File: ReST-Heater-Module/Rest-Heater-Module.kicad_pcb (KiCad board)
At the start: 2 copper layers, 17.4 x 34.4 mm, 62 parts, among them P1 CONN_02X02, P2 CONN_02X05, P3 02-SCREW-TERM, P4 01X02-MALE, P5 02-SCREW-TERM, Q1 Q_BSH105, Q2 Q_AOT240L

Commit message: Save of work
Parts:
- added JP***: bb02-hp04, ReST-Library:bb02-hp04, B.Cu at (144.0, 109.6)
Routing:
- net +12V: track 49.9 -> 2.49 mm
- added copper zone on B.Cu, net +12V
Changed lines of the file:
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@@
 (kicad_pcb (version 4) (host pcbnew 4.0.2-stable)
   (general
-    (links 79)
+    (links 83)
     (no_connects 0)
     (area 140.794999 97.794999 158.205001 132.205001)
     (thickness 1.6)
     (drawings 14)
-    (tracks 158)
+    (tracks 140)
     (zones 0)
-    (modules 62)
+    (modules 63)
     (nets 11)
   )
@@
   )
   (setup
-    (last_trace_width 0.3)
+    (last_trace_width 0.25)
     (user_trace_width 0.2)
     (user_trace_width 0.3)
@@
     (mod_text_size 1 1)
     (mod_text_width 0.15)
-    (pad_size 0.5 0.5)
-    (pad_drill 0.4)
+    (pad_size 1.02 3.45)
+    (pad_drill 0)
     (pad_to_mask_clearance 0)
     (aux_axis_origin 0 0)
@@
     )
     (model ../../../../../../Users/Matjas/Documents/Git/RepRapSTM32duinoDriver/3D-Models/conn_mpt/mpt_0,5-2-2,54.wrl
+      (at (xyz 0 0 0))
+      (scale (xyz 1 1 1))
+      (rotate (xyz 0 0 0))
+    )
+  )
+  (module ReST-Library:bb02-hp04 (layer B.Cu)
+    (at 144 109.6)
+    (descr "Smd dual-row strip connector, 2x2 pin, 2.54mm pitch")
+    (fp_text reference JP*** (at 0 5.2) (layer B.SilkS)
+      (effects (font (size 0.99822 0.99822) (thickness 0.19812)) (justify mirror))
+    )
+    (fp_text value bb02-hp04 (at 0 -5.5) (layer B.SilkS)
+      (effects (font (size 0.99568 0.99568) (thickness 0.19558)) (justify mirror))
+    )
+    (fp_text user 1 (at -1.2 -0.4 270) (layer B.SilkS)
+      (effects (font (size 1 1) (thickness 0.15)) (justify mirror))
+    )
+    (fp_line (start -2.6 2.6) (end 2.6 2.6) (layer B.SilkS) (width 0.19812))
+    (fp_line (start 2.6 2.6) (end 2.6 -2.6) (layer B.SilkS) (width 0.19812))
+    (fp_line (start 2.6 -2.6) (end -2.6 -2.6) (layer B.SilkS) (width 0.19812))
+    (fp_line (start -2.6 -2.6) (end -2.6 2.6) (layer B.SilkS) (width 0.19812))
+    (pad 1 smd rect (at -1.27 -2.725) (size 1.02 3.45) (layers B.Cu B.Paste B.Mask)
+      (net 5 +12V))
+    (pad 2 smd rect (at -1.27 2.725) (size 1.02 3.45) (layers B.Cu B.Paste B.Mask)
+      (net 5 +12V))
+    (pad 3 smd rect (at 1.27 -2.725) (size 1.02 3.45) (layers B.Cu B.Paste B.Mask)
+      (net 5 +12V))
+    (pad 4 smd rect (at 1.27 2.725) (size 1.02 3.45) (layers B.Cu B.Paste B.Mask)
+      (net 5 +12V))
+    (model walter/smd_strip/BB02-HP04.wrl
       (at (xyz 0 0 0))
       (scale (xyz 1 1 1))
@@
   (segment (start 147.41986 124.41986) (end 144.10008 121.10008) (width 0.3) (layer F.Cu) (net 4))
   (segment (start 144.10008 121.10008) (end 144 121.10008) (width 0.3) (layer F.Cu) (net 4))
-  (segment (start 149.5095 122.9595) (end 150 122.9595) (width 3) (layer B.Cu) (net 5))
-  (segment (start 150 122.9595) (end 149.5095 122.9595) (width 3) (layer B.Cu) (net 5))
-  (segment (start 149.5095 122.9595) (end 144.92254 118.37254) (width 3) (layer B.Cu) (net 5))
   (via (at 144.45 123.15) (size 0.6) (drill 0.4) (layers F.Cu B.Cu) (net 5))
   (segment (start 144.45 123.15) (end 144.6405 122.9595) (width 1.5) (layer B.Cu) (net 5))
   (segment (start 144.6405 122.9595) (end 144.92254 122.9595) (width 1.5) (layer B.Cu) (net 5))
-  (segment (start 147.46 115.53) (end 147.46 120.91) (width 3) (layer B.Cu) (net 5))
-  (segment (start 147.46 120.91) (end 149.5095 122.9595) (width 3) (layer B.Cu) (net 5))
-  (segment (start 147.46 122.9595) (end 150 122.9595) (width 3) (layer B.Cu) (net 5))
-  (segment (start 144.92254 122.9595) (end 144.92254 118.37254) (width 3) (layer B.Cu) (net 5))
-  (segment (start 144.92254 118.37254) (end 144.92254 116.62254) (width 3) (layer B.Cu) (net 5))
-  (segment (start 144.92254 116.62254) (end 144.9 116.64508) (width 3) (layer B.Cu) (net 5))
-  (segment (start 144.9 116.64508) (end 144.9 118.5) (width 3) (layer B.Cu) (net 5))
-  (segment (start 147.46 122.9595) (end 144.92254 122.9595) (width 3) (layer B.Cu) (net 5))
-  (segment (start 144.92 115.53) (end 144.92 118.5) (width 5) (layer B.Cu) (net 5))
-  (segment (start 144.92 118.5) (end 144.92 116.62) (width 5) (layer B.Cu) (net 5))
-  (segment (start 144.92 115.53) (end 144.92 115.47) (width 5) (layer B.Cu) (net 5))
-  (segment (start 144.92 115.47) (end 144.05 114.6) (width 5) (layer B.Cu) (net 5))
   (segment (start 144 124.89992) (end 144 123.6) (width 1.5) (layer F.Cu) (net 5))
   (segment (start 144 123.6) (end 144.45 123.15) (width 1.5) (layer F.Cu) (net 5))
-  (segment (start 144.9 118.5) (end 144.92 118.5) (width 3) (layer B.Cu) (net 5))
-  (segment (start 144.05 114.6) (end 144.05 102.7) (width 5) (layer B.Cu) (net 5))
-  (segment (start 144.05 102.7) (end 144.25 102.5) (width 5) (layer B.Cu) (net 5))
   (segment (start 145.925 131.35) (end 144.475 131.35) (width 0.3) (layer B.Cu) (net 6))
   (segment (start 144.4 125.8) (end 144.975 125.225) (width 0.3) (layer B.Cu) (net 6))
@@
     (connect_pads (clearance 0.35))
     (min_thickness 0.254)
-    (fill yes (arc_segments 16) (thermal_gap 0.508) (thermal_bridge_width 1))
+    (fill yes (arc_segments 16) (thermal_gap 0.508) (thermal_bridge_width 2))
     (polygon
       (pts
@@
     (connect_pads (clearance 0.35))
     (min_thickness 0.254)
-    (fill yes (arc_segments 16) (thermal_gap 0.508) (thermal_bridge_width 1))
+    (fill yes (arc_segments 16) (thermal_gap 0.508) (thermal_bridge_width 2))
     (polygon
       (pts
@@
       )
     )
+  )
+  (zone (net 5) (net_name +12V) (layer B.Cu) (hatch edge 0.508)
+    (priority 1)
+    (connect_pads yes (clearance 0.35))
+    (min_thickness 0.254)
+    (fill yes (arc_segments 16) (thermal_gap 0.508) (thermal_bridge_width 2))
+    (polygon
+      (pts
+        (xy 151 124.2) (xy 142.2 124.2) (xy 142.2 116.4) (xy 141.6 115.8) (xy 141.6 101.2)
+        (xy 143.2 99.6) (xy 145.6 99.6) (xy 147 101) (xy 147 104.2) (xy 146.6 104.6)
+        (xy 146.6 113) (xy 147.4 113.8) (xy 148.6 113.8) (xy 148.6 119.2) (xy 151 119.2)
+      )
+    )

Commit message: finishing touches on Heater and Stepper Modules
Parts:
- C1: value 10uF -> (none)
- D1: value LED -> (none)
- D2: value D_1N400x-SMD -> (none)
- P1: value CONN_02X02 -> (none)
- P3, P5: value 02-SCREW-TERM -> (none)
- P4: value 01X02-MALE -> (none)
- Q1: value Q_BSH105 -> (none)
- Q2: value Q_AOT240L -> (none)
- R1: value 4.7K -> (none)
- R2, R3: value 100K -> (none)
- R4: value 22R -> (none)
- R5: value 1K -> (none)
- renumbered JP*** to P7

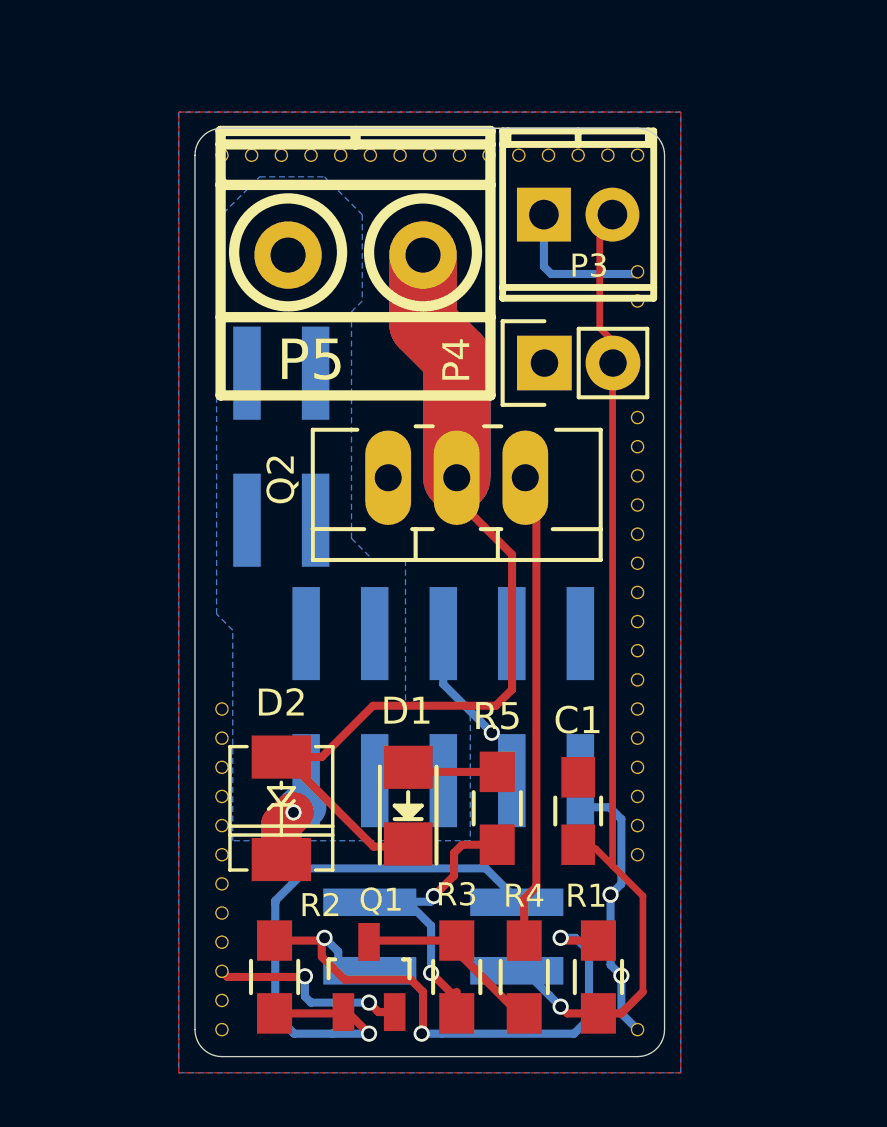
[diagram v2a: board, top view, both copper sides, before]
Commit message: Changes in Heatbed and Heater + F1 and F4 Pinout table with functions
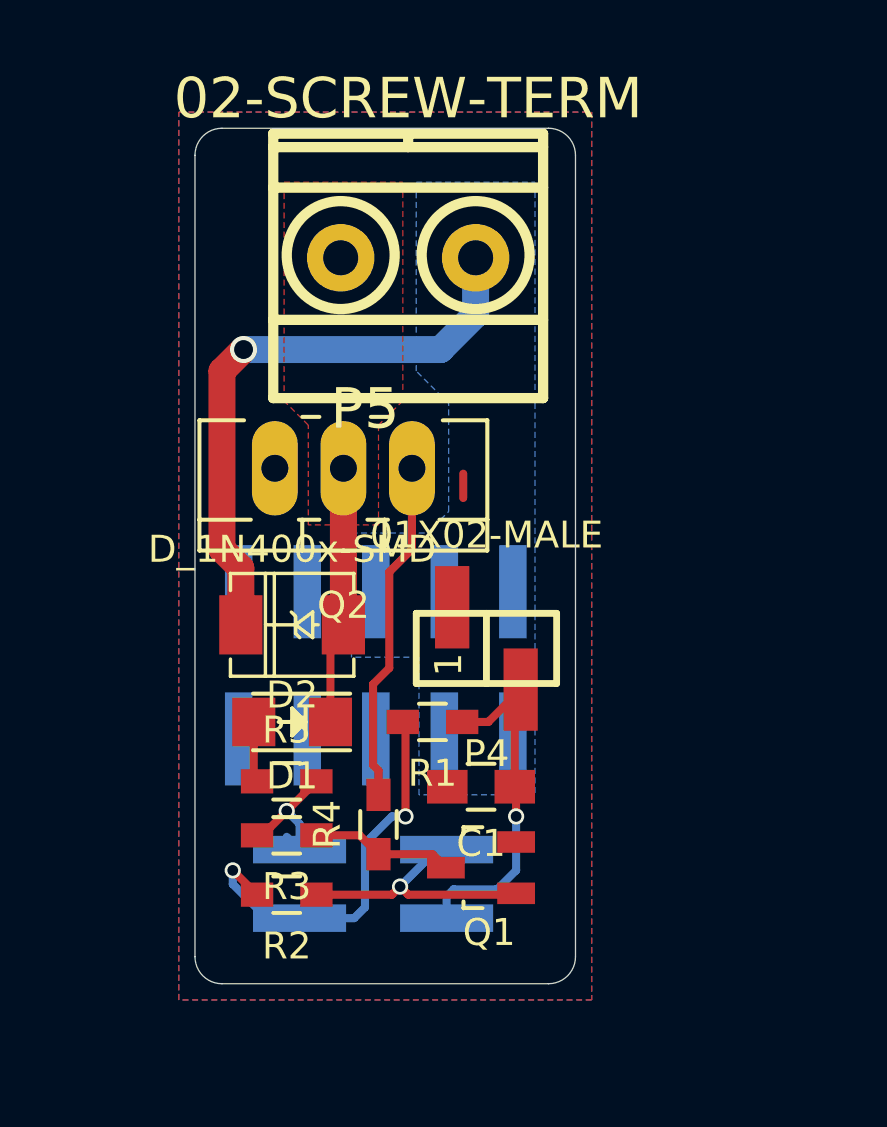
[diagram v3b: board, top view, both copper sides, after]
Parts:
- removed ? (x47): , ReST-Library:1pin
- removed P3: , ReST-Library:screw-2.54-2P
- removed P7: bb02-hp04, ReST-Library:bb02-hp04
- C1: value (none) -> 10uF
- D1: value (none) -> LED
- D2: value (none) -> D_1N400x-SMD
- P1: value (none) -> CONN_02X02
- P4: value (none) -> 01X02-MALE; footprint Pin_Headers:Pin_Header_Straight_1x02 -> ReST-Library:bb02-hy02a
- P5: value (none) -> 02-SCREW-TERM
- Q1: value (none) -> Q_BSH105
- Q2: value (none) -> Q_AOT240L
- R1: value (none) -> 4.7K; footprint Resistors_SMD:R_0805_HandSoldering -> Resistors_SMD:R_0603_HandSoldering
- R2, R3: value (none) -> 100K; footprint Resistors_SMD:R_0805_HandSoldering -> Resistors_SMD:R_0603_HandSoldering
- R4: value (none) -> 22R; footprint Resistors_SMD:R_0805_HandSoldering -> Resistors_SMD:R_0603_HandSoldering
- R5: value (none) -> 1K; footprint Resistors_SMD:R_0805_HandSoldering -> Resistors_SMD:R_0603_HandSoldering
- moved R1 11.3 mm to (149.6, 119.8), turned to 180 degrees
- moved P4 10.8 mm to (151.6, 117.1), turned to 180 degrees
- moved R3 8.20 mm to (144.2, 124.0), turned to 180 degrees
- moved R5 7.86 mm to (144.2, 122.0), turned to 0 degrees
- moved R4 7.82 mm to (147.6, 123.6)
- moved D2 6.81 mm to (144.4, 116.2), turned to 180 degrees
- moved Q1 5.80 mm to (151.4, 125.2), turned to 90 degrees
- moved D1 5.30 mm to (144.4, 119.8), turned to 180 degrees
- moved Q2 4.21 mm to (146.3, 110.4)
- moved C1 3.71 mm to (151.4, 122.2), turned to 180 degrees
- moved P1 3.25 mm to (147.4, 125.8)
- moved R2 3.08 mm to (144.2, 126.2), turned to 180 degrees
- moved P2 2.94 mm to (147.5, 117.7)
- moved P5 1.95 mm to (148.7, 102.6)
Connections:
- D1 pad 1: Net-(D1-Pad1) -> /PWM
- D2 pad 2: Net-(D1-Pad1) -> /PWM
- P2 pad 1: +12V -> GND
- P2 pad 10: GND -> +12V
- P2 pad 2: +12V -> GND
- P2 pad 3: +12V -> GND
- P2 pad 4: +12V -> GND
- P2 pad 5: GND -> +12V
- P2 pad 6: +12V -> GND
- P2 pad 7: GND -> +12V
- P2 pad 8: GND -> +12V
- P2 pad 9: GND -> +12V
- P5 pad 1: Net-(D1-Pad1) -> +12V
- P5 pad 2: +12V -> /PWM
- Q2 pad 2: Net-(D1-Pad1) -> /PWM
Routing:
- net Net-(D1-Pad1): track 41.9 -> 0.00 mm
- net GND: track 28.5 -> 0.00 mm, vias 5 -> 0
- net /T1: track 36.9 -> 13.3 mm
- net +12V: track 2.49 -> 22.1 mm
- net /PWM-HEATER: track 24.0 -> 9.96 mm
- net /PWM: track 0.00 -> 9.60 mm
- net +5V: track 15.1 -> 5.53 mm, vias 2 -> 1
- net +3V3: track 21.7 -> 15.2 mm, vias 3 -> 2
- net Net-(Q2-Pad1): track 17.5 -> 12.8 mm
- net Net-(Q1-Pad3): track 7.12 -> 5.30 mm
- net Net-(D1-Pad2): track 3.28 -> 2.25 mm
- net (no net): track 0.00 -> 0.90 mm
- added copper zone on F.Cu, net /PWM
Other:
- board size 17.4 x 34.4 mm -> 14.1 x 31.7 mm
